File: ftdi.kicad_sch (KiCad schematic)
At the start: 44 parts, among them U1 93LC56BT-I/OT

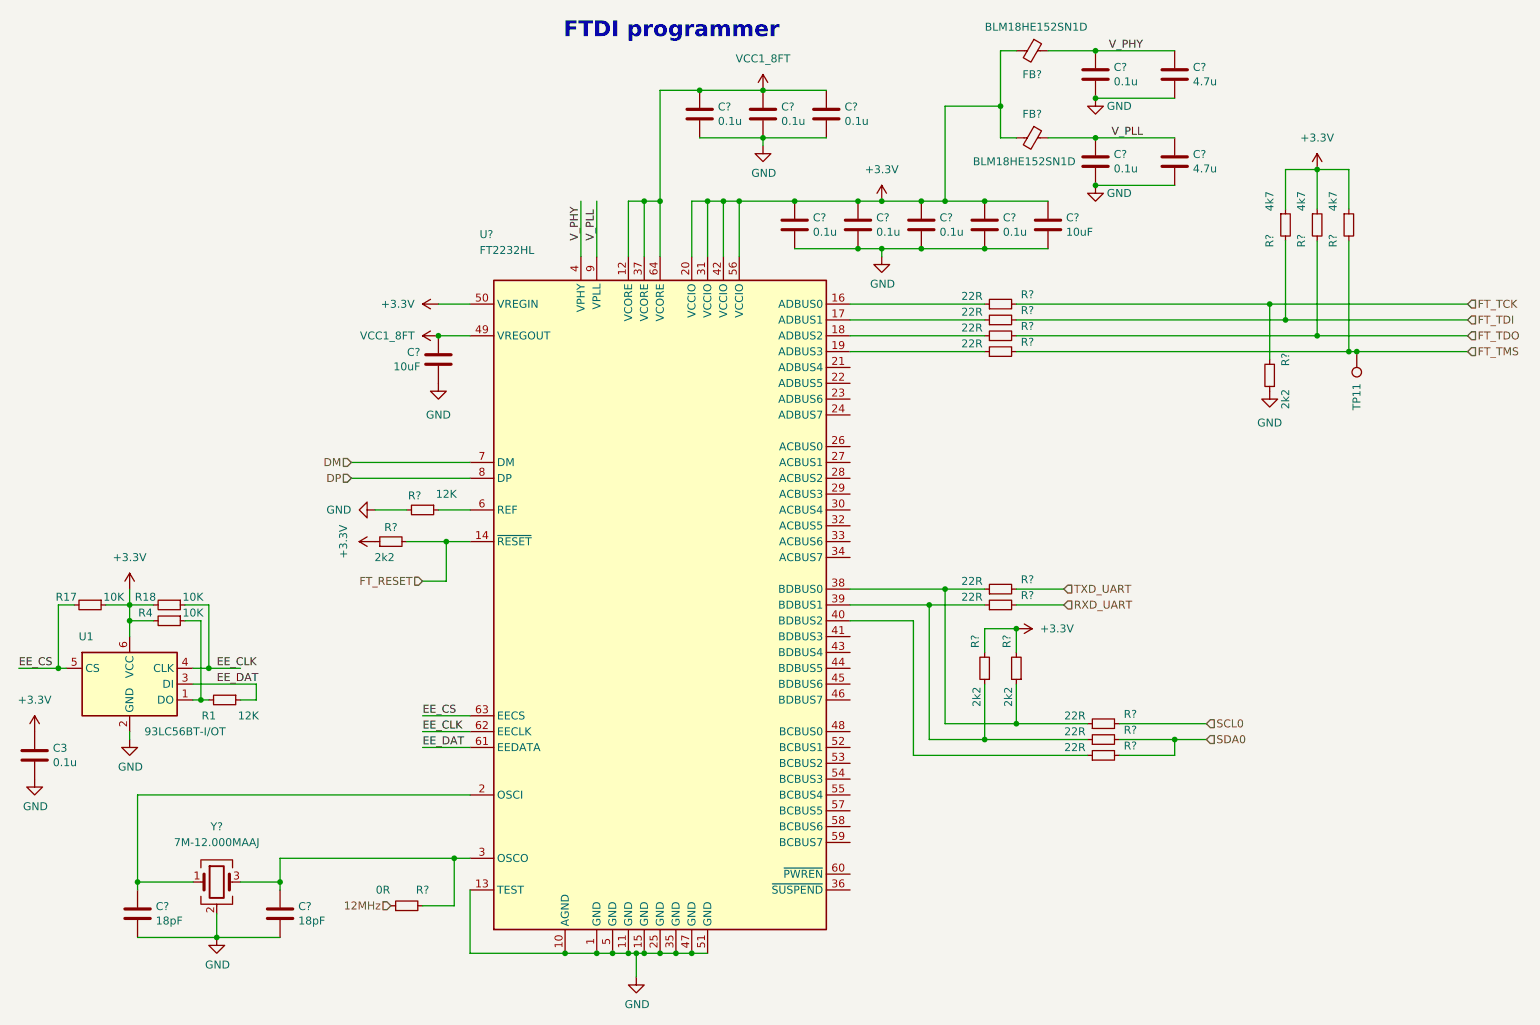
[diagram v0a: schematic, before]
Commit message: start to assign footprint
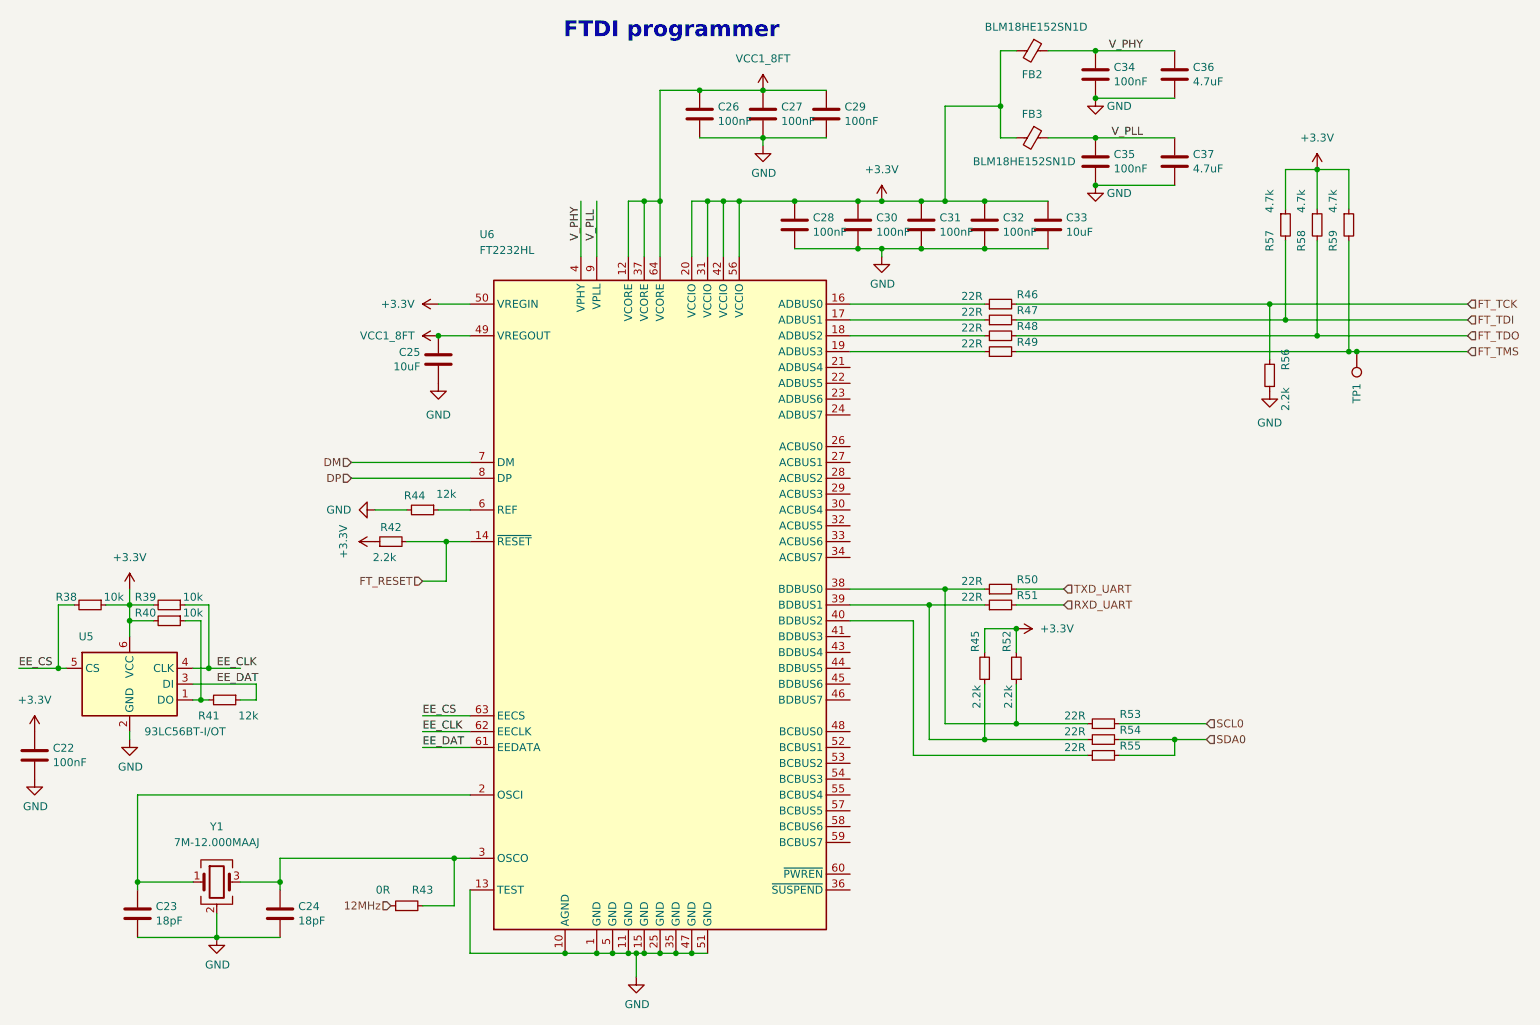
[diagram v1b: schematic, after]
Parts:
- C22: renamed from C3; value 0.1u -> 100nF
- C25, C33: renamed from C?; footprint Capacitor_SMD:C_0402_1005Metric -> Capacitor_SMD:C_1206_3216Metric
- C26, C27, C28, C29, C30, C31, C32, C34, C35: renamed from C?; value 0.1u -> 100nF
- C36, C37: renamed from C?; value 4.7u -> 4.7uF; footprint Capacitor_SMD:C_0603_1608Metric -> Capacitor_SMD:C_0805_2012Metric
- R38: renamed from R17; value 10K -> 10k
- R39: renamed from R18; value 10K -> 10k
- R40: renamed from R4; value 10K -> 10k
- R41: renamed from R1; value 12K -> 12k
- R42, R45, R52, R56: renamed from R?; value 2k2 -> 2.2k
- R44: renamed from R?; value 12K -> 12k
- R57, R58, R59: renamed from R?; value 4k7 -> 4.7k
- Y1: renamed from Y?; footprint (none) -> Oscillator:Oscillator_SMD_Abracon_ASE-4Pin_3.2x2.5mm
- gave numbers to parts that had none: 15
- renumbered TP11 to TP1, U1 to U5

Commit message: Assign jlcpcb pn. Fix footprint assign, uniform resistor value for battery charger
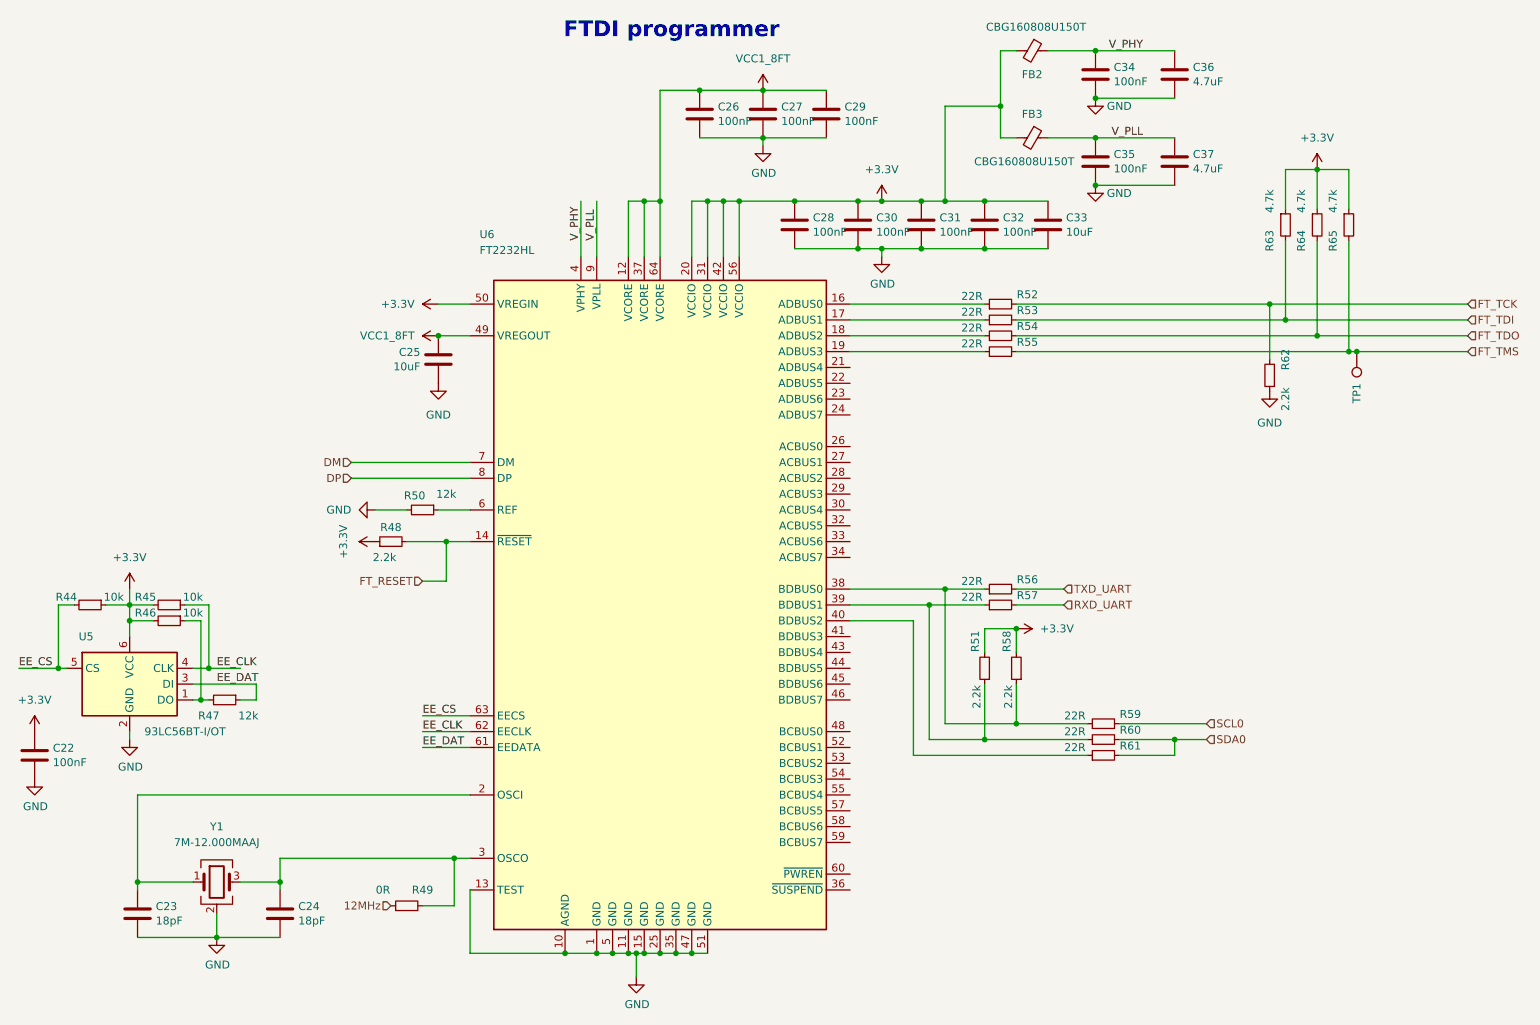
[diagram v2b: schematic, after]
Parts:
- FB2, FB3: value BLM18HE152SN1D -> CBG160808U150T
- U5: footprint vs:SOT-23-6 -> Package_TO_SOT_SMD:SOT-23-6
- renumbered R38 to R44, R39 to R45, R40 to R46, R41 to R47, R42 to R48, R43 to R49, R44 to R50, R45 to R51, R46 to R52, R47 to R53, R48 to R54, R49 to R55, R50 to R56, R51 to R57, R52 to R58, R53 to R59, R54 to R60, R55 to R61, R56 to R62, R57 to R63, R58 to R64, R59 to R65

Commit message: routing sram
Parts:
- FB3: LCSC (none) -> C98495
- R49: LCSC (none) -> C21189
- R50: LCSC (none) -> C22790
- R60, R65: Mfg (none) -> ‎Yageo‎; Mfg_1 (none) -> UNI-ROYAL(Uniroyal Elec); PN (none) -> RC0201FR-074K7L; PN_1 (none) -> 0201WMF4701TCE
- R61, R62, R63, R64: Mfg (none) -> ‎Yageo‎; Mfg_1 (none) -> UNI-ROYAL(Uniroyal Elec); PN (none) -> RC0201FR-0720RL; PN_1 (none) -> 0201WMF200JTCE
- U5: LCSC (none) -> C190271
- Y1: private KLC_S4.1 -> (none)

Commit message: Routing sram
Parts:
- R52, R53, R54, R55, R56, R57, R59, R60, R61: footprint Resistor_SMD:R_0603_1608Metric -> Resistor_SMD:R_01005_0402Metric_Pad0.57x0.30mm_HandSolder
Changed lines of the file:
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@@
 			)
 		)
-		(property "Footprint" "Resistor_SMD:R_0603_1608Metric"
+		(property "Footprint" "Resistor_SMD:R_01005_0402Metric_Pad0.57x0.30mm_HandSolder"
 			(at 176.53 82.55 0)
 			(effects
@@
 			)
 		)
-		(property "Footprint" "Resistor_SMD:R_0603_1608Metric"
+		(property "Footprint" "Resistor_SMD:R_01005_0402Metric_Pad0.57x0.30mm_HandSolder"
 			(at 193.04 147.32 0)
 			(effects
@@
 			)
 		)
-		(property "Footprint" "Resistor_SMD:R_0603_1608Metric"
+		(property "Footprint" "Resistor_SMD:R_01005_0402Metric_Pad0.57x0.30mm_HandSolder"
 			(at 176.53 120.65 0)
 			(effects
@@
 			)
 		)
-		(property "Footprint" "Resistor_SMD:R_0603_1608Metric"
+		(property "Footprint" "Resistor_SMD:R_01005_0402Metric_Pad0.57x0.30mm_HandSolder"
 			(at 176.53 80.01 0)
 			(effects
@@
 			)
 		)
-		(property "Footprint" "Resistor_SMD:R_0603_1608Metric"
+		(property "Footprint" "Resistor_SMD:R_01005_0402Metric_Pad0.57x0.30mm_HandSolder"
 			(at 193.04 144.78 0)
 			(effects
@@
 			)
 		)
-		(property "Footprint" "Resistor_SMD:R_0603_1608Metric"
+		(property "Footprint" "Resistor_SMD:R_01005_0402Metric_Pad0.57x0.30mm_HandSolder"
 			(at 176.53 77.47 0)
 			(effects
@@
 			)
 		)
-		(property "Footprint" "Resistor_SMD:R_0603_1608Metric"
+		(property "Footprint" "Resistor_SMD:R_01005_0402Metric_Pad0.57x0.30mm_HandSolder"
 			(at 176.53 74.93 0)
 			(effects
@@
 			)
 		)
-		(property "Footprint" "Resistor_SMD:R_0603_1608Metric"
+		(property "Footprint" "Resistor_SMD:R_01005_0402Metric_Pad0.57x0.30mm_HandSolder"
 			(at 176.53 123.19 0)
 			(effects
@@
 			)
 		)
-		(property "Footprint" "Resistor_SMD:R_0603_1608Metric"
+		(property "Footprint" "Resistor_SMD:R_01005_0402Metric_Pad0.57x0.30mm_HandSolder"
 			(at 193.04 142.24 0)
 			(effects

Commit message: Complete SRAM, and routing VGA
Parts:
- R52, R53, R54, R55, R56, R57, R59, R60, R61: footprint Resistor_SMD:R_01005_0402Metric_Pad0.57x0.30mm_HandSolder -> Resistor_SMD:R_0402_1005Metric_Pad0.72x0.64mm_HandSolder
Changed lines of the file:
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@@
 			)
 		)
-		(property "Footprint" "Resistor_SMD:R_01005_0402Metric_Pad0.57x0.30mm_HandSolder"
+		(property "Footprint" "Resistor_SMD:R_0402_1005Metric_Pad0.72x0.64mm_HandSolder"
 			(at 176.53 82.55 0)
 			(effects
@@
 			)
 		)
-		(property "Footprint" "Resistor_SMD:R_01005_0402Metric_Pad0.57x0.30mm_HandSolder"
+		(property "Footprint" "Resistor_SMD:R_0402_1005Metric_Pad0.72x0.64mm_HandSolder"
 			(at 193.04 147.32 0)
 			(effects
@@
 			)
 		)
-		(property "Footprint" "Resistor_SMD:R_01005_0402Metric_Pad0.57x0.30mm_HandSolder"
+		(property "Footprint" "Resistor_SMD:R_0402_1005Metric_Pad0.72x0.64mm_HandSolder"
 			(at 176.53 120.65 0)
 			(effects
@@
 			)
 		)
-		(property "Footprint" "Resistor_SMD:R_01005_0402Metric_Pad0.57x0.30mm_HandSolder"
+		(property "Footprint" "Resistor_SMD:R_0402_1005Metric_Pad0.72x0.64mm_HandSolder"
 			(at 176.53 80.01 0)
 			(effects
@@
 			)
 		)
-		(property "Footprint" "Resistor_SMD:R_01005_0402Metric_Pad0.57x0.30mm_HandSolder"
+		(property "Footprint" "Resistor_SMD:R_0402_1005Metric_Pad0.72x0.64mm_HandSolder"
 			(at 193.04 144.78 0)
 			(effects
@@
 			)
 		)
-		(property "Footprint" "Resistor_SMD:R_01005_0402Metric_Pad0.57x0.30mm_HandSolder"
+		(property "Footprint" "Resistor_SMD:R_0402_1005Metric_Pad0.72x0.64mm_HandSolder"
 			(at 176.53 77.47 0)
 			(effects
@@
 			)
 		)
-		(property "Footprint" "Resistor_SMD:R_01005_0402Metric_Pad0.57x0.30mm_HandSolder"
+		(property "Footprint" "Resistor_SMD:R_0402_1005Metric_Pad0.72x0.64mm_HandSolder"
 			(at 176.53 74.93 0)
 			(effects
@@
 			)
 		)
-		(property "Footprint" "Resistor_SMD:R_01005_0402Metric_Pad0.57x0.30mm_HandSolder"
+		(property "Footprint" "Resistor_SMD:R_0402_1005Metric_Pad0.72x0.64mm_HandSolder"
 			(at 176.53 123.19 0)
 			(effects
@@
 			)
 		)
-		(property "Footprint" "Resistor_SMD:R_01005_0402Metric_Pad0.57x0.30mm_HandSolder"
+		(property "Footprint" "Resistor_SMD:R_0402_1005Metric_Pad0.72x0.64mm_HandSolder"
 			(at 193.04 142.24 0)
 			(effects

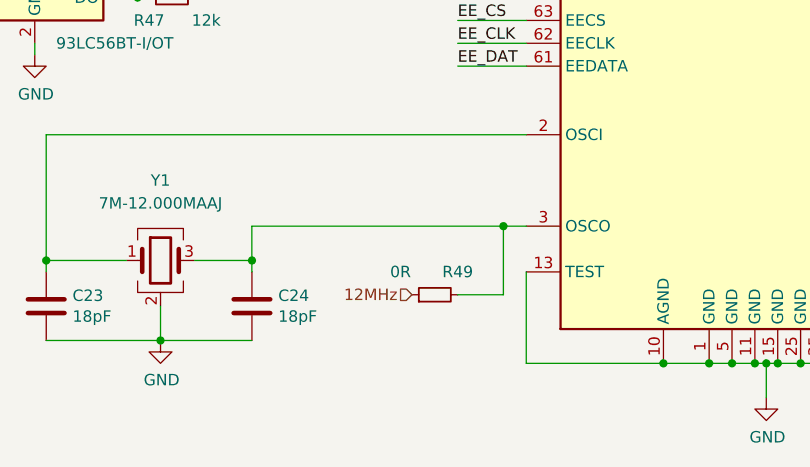
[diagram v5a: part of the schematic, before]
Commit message: Place db9, encoder, btn and leds. Continue routing.
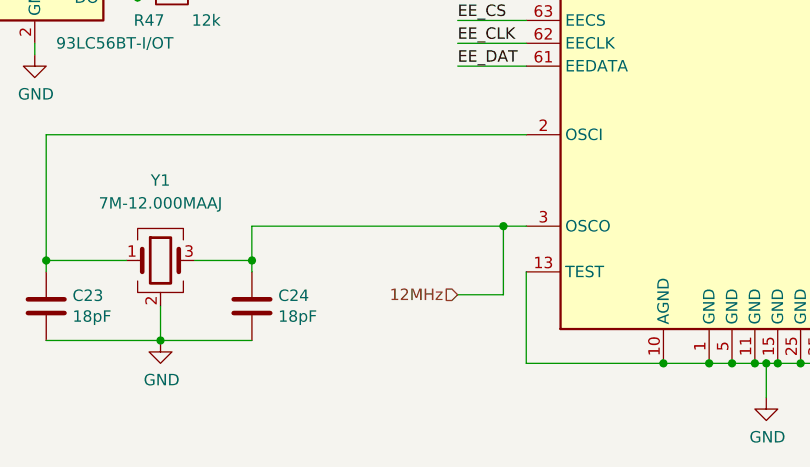
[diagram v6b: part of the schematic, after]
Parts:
- removed R49: 0R, Resistor_SMD:R_0603_1608Metric, symbol UPduino_v3.0:Device_R_Small
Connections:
- net 12MHz: now also C24.1, U6.3 (OSCO), Y1.3
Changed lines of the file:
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@@
 	(hierarchical_label "12MHz"
 		(shape input)
-		(at 78.74 171.45 180)
+		(at 83.82 171.45 180)
 		(effects
 			(font
@@
 					(unit 1)
 				)
-			)
-		)
-	)
-	(symbol
-		(lib_id "UPduino_v3.0:Device_R_Small")
-		(at 81.28 171.45 90)
-		(unit 1)
-		(exclude_from_sim no)
-		(in_bom yes)
-		(on_board yes)
-		(dnp no)
-		(property "Reference" "R49"
-			(at 83.82 168.91 90)
-			(effects
-				(font
-					(size 1.27 1.27)
-				)
-			)
-		)
-		(property "Value" "0R"
-			(at 77.47 168.91 90)
-			(effects
-				(font
-					(size 1.27 1.27)
-				)
-			)
-		)
-		(property "Footprint" "Resistor_SMD:R_0603_1608Metric"
-			(at 81.28 171.45 0)
-			(effects
-				(font
-					(size 1.27 1.27)
-				)
-				(hide yes)
-			)
-		)
-		(property "Datasheet" "~"
-			(at 81.28 171.45 0)
-			(effects
-				(font
-					(size 1.27 1.27)
-				)
-				(hide yes)
-			)
-		)
-		(property "Description" ""
-			(at 81.28 171.45 0)
-			(effects
-				(font
-					(size 1.27 1.27)
-				)
-				(hide yes)
-			)
-		)
-		(property "KLC_S3.3" ""
-			(at 81.28 171.45 90)
-			(effects
-				(font
-					(size 1.27 1.27)
-				)
-				(hide yes)
-			)
-		)
-		(property "KLC_S4.1" ""
-			(at 81.28 171.45 90)
-			(effects
-				(font
-					(size 1.27 1.27)
-				)
-				(hide yes)
-			)
-		)
-		(property "LCSC" "C21189"
-			(at 81.28 171.45 0)
-			(effects
-				(font
-					(size 1.27 1.27)
-				)
-				(hide yes)
-			)
-		)
-		(pin "1"
-		)
-		(pin "2"
-		)
-		(instances
-			(project "fpgaler"
-				(path "/d6c42660-1080-4fbd-a2d9-2a0cd6b4e770/40d0c523-fc24-4097-9888-0fa62d687751"
-					(reference "R49")
-					(unit 1)
-				)

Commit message: Continue routing
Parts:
- removed TP1: TestPoint, TestPoint:TestPoint_Pad_D1.0mm, symbol UPduino_v3.0:Connector_TestPoint
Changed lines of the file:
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@@
-	)
-	(junction
-		(at 233.68 82.55)
-		(diameter 0)
-		(color 0 0 0 0)
 	)
 	(junction
@@
 	(wire
 		(pts
-			(xy 233.68 82.55) (xy 251.46 82.55)
+			(xy 232.41 82.55) (xy 251.46 82.55)
 		)
 		(stroke
@@
 		(pts
 			(xy 176.53 34.29) (xy 176.53 43.18)
-		)
-		(stroke
-			(width 0)
-			(type default)
-		)
-	)
-	(wire
-		(pts
-			(xy 232.41 82.55) (xy 233.68 82.55)
 		)
 		(stroke
@@
 					(unit 1)
 				)
-			)
-		)
-	)
-	(symbol
-		(lib_id "UPduino_v3.0:Connector_TestPoint")
-		(at 233.68 82.55 180)
-		(unit 1)
-		(exclude_from_sim no)
-		(in_bom yes)
-		(on_board yes)
-		(dnp no)
-		(property "Reference" "TP1"
-			(at 233.68 87.63 90)
-			(effects
-				(font
-					(size 1.27 1.27)
-				)
-				(justify left)
-			)
-		)
-		(property "Value" "TestPoint"
-			(at 232.537 87.3252 90)
-			(effects
-				(font
-					(size 1.27 1.27)
-				)
-				(justify left)
-				(hide yes)
-			)
-		)
-		(property "Footprint" "TestPoint:TestPoint_Pad_D1.0mm"
-			(at 228.6 82.55 0)
-			(effects
-				(font
-					(size 1.27 1.27)
-				)
-				(hide yes)
-			)
-		)
-		(property "Datasheet" "~"
-			(at 228.6 82.55 0)
-			(effects
-				(font
-					(size 1.27 1.27)
-				)
-				(hide yes)
-			)
-		)
-		(property "Description" ""
-			(at 233.68 82.55 0)
-			(effects
-				(font
-					(size 1.27 1.27)
-				)
-				(hide yes)
-			)
-		)
-		(property "KLC_S3.3" ""
-			(at 233.68 82.55 90)
-			(effects
-				(font
-					(size 1.27 1.27)
-				)
-				(hide yes)
-			)
-		)
-		(property "KLC_S4.1" ""
-			(at 233.68 82.55 90)
-			(effects
-				(font
-					(size 1.27 1.27)
-				)
-				(hide yes)
-			)
-		)
-		(pin "1"
-		)
-		(instances
-			(project "fpgaler"
-				(path "/d6c42660-1080-4fbd-a2d9-2a0cd6b4e770/40d0c523-fc24-4097-9888-0fa62d687751"
-					(reference "TP1")
-					(unit 1)
-				)

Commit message: Start routing pwr
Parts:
- FB2, FB3: value CBG160808U150T -> 15Ω@100MHz; footprint Inductor_SMD:L_0603_1608Metric -> Inductor_SMD:L_0603_1608Metric_Pad1.05x0.95mm_HandSolder
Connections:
- net DM renamed D_N
- net DP renamed D_P
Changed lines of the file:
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@@
 		)
 	)
-	(hierarchical_label "DP"
+	(hierarchical_label "D_P"
 		(shape input)
 		(at 72.39 102.87 180)
@@
 			(justify right)
 		)
+		(property "Netclass" "diff90"
+			(at 78.74 101.6 0)
+			(effects
+				(font
+					(size 1.27 1.27)
+					(italic yes)
+				)
+				(justify right)
+			)
+		)
 	)
 	(hierarchical_label "FT_RESET"
@@
 		)
 	)
-	(hierarchical_label "DM"
+	(hierarchical_label "D_N"
 		(shape input)
 		(at 72.39 100.33 180)
@@
 			(justify right)
 		)
+		(property "Netclass" "diff90"
+			(at 78.74 99.06 0)
+			(effects
+				(font
+					(size 1.27 1.27)
+					(italic yes)
+				)
+				(justify right)
+			)
+		)
 	)
 	(hierarchical_label "FT_TDO"
@@
 			)
 		)
-		(property "Value" "CBG160808U150T"
+		(property "Value" "15Ω@100MHz"
 			(at 180.34 52.07 90)
 			(effects
@@
 			)
 		)
-		(property "Footprint" "Inductor_SMD:L_0603_1608Metric"
+		(property "Footprint" "Inductor_SMD:L_0603_1608Metric_Pad1.05x0.95mm_HandSolder"
 			(at 181.61 46.482 90)
 			(effects
@@
 			)
 		)
-		(property "Description" ""
+		(property "Description" "CBG160808U150T"
 			(at 181.61 48.26 0)
 			(effects
@@
 			)
 		)
-		(property "Value" "CBG160808U150T"
+		(property "Value" "15Ω@100MHz"
 			(at 182.245 30.48 90)
 			(effects
@@
 			)
 		)
-		(property "Footprint" "Inductor_SMD:L_0603_1608Metric"
+		(property "Footprint" "Inductor_SMD:L_0603_1608Metric_Pad1.05x0.95mm_HandSolder"
 			(at 181.61 32.512 90)
 			(effects
@@
 			)
 		)
-		(property "Description" ""
+		(property "Description" "CBG160808U150T"
 			(at 181.61 34.29 0)
 			(effects
